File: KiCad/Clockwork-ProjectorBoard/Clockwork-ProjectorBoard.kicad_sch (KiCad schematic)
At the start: 32 parts, among them J1 to TCA955 PCB, J2 to DIN connecting 3+1 Socket 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, J3 to Lamp Relay Board, J4 to DIN Socket traces, J5 Relais Board, J6 uC Cable, J7 DIN-6 female, Q1 AO3400A, U1 AP63205WU, U3 TS5A3160DBVR-TP, U4 TS5A3160DBVR-TP, U5 TSV911ILT

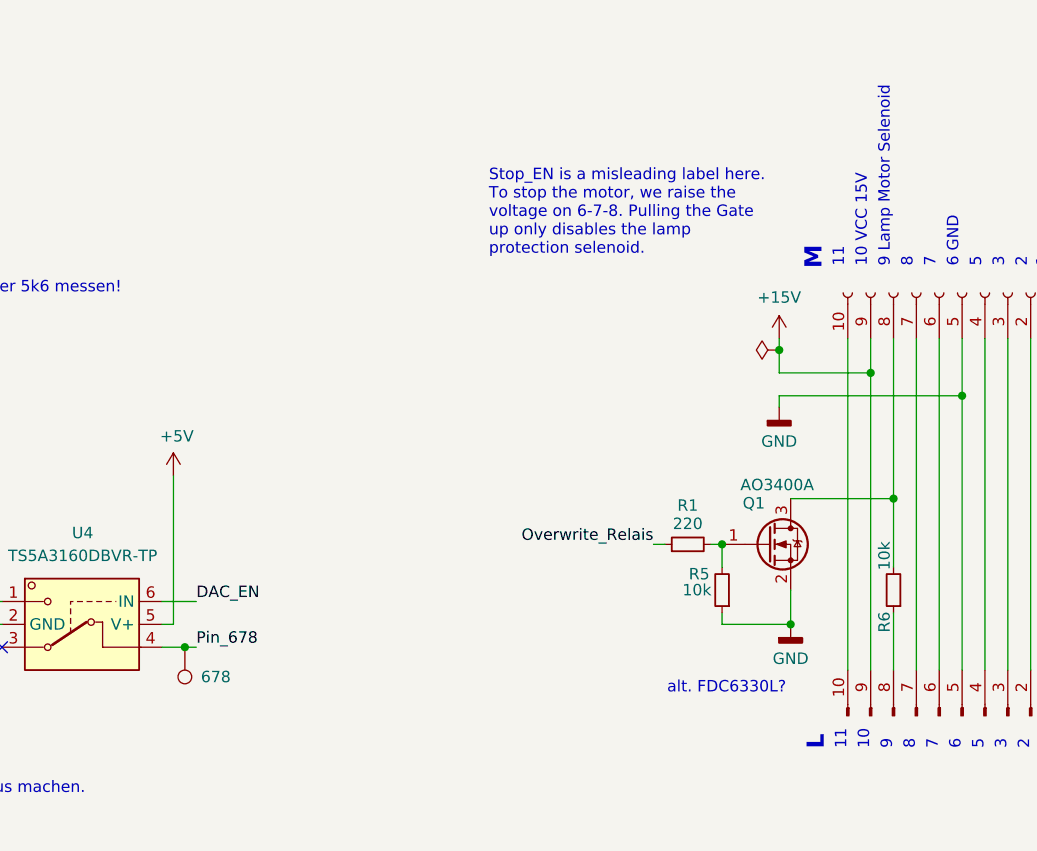
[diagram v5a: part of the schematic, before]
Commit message: Optimize Projector Board Size, red socket will fit better.
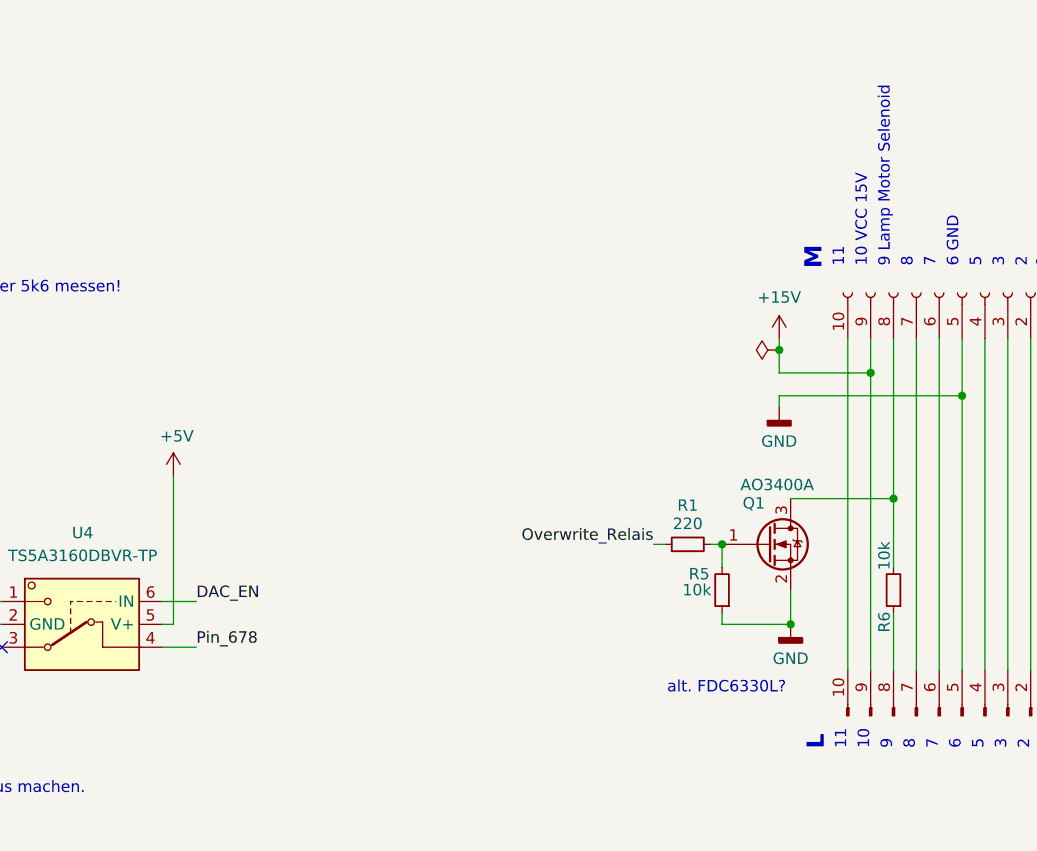
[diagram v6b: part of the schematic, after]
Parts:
- removed TP1: 678, TestPoint:TestPoint_Pad_D1.0mm, symbol Peacemans Teile:TestPoint_named
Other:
- note removed: "Stop_EN is a misleading label here. To stop the motor, we raise the voltage on 6-7-8. Pulling the Gate up only disables the lamp protection selenoid."
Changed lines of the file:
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@@
 	)
 	(junction
-		(at 167.64 130.81)
-		(diameter 0)
-		(color 0 0 0 0)
-	)
-	(junction
 		(at 152.4 43.18)
 		(diameter 0)
@@
 	(wire
 		(pts
-			(xy 168.91 130.81) (xy 167.64 130.81)
+			(xy 165.1 130.81) (xy 168.91 130.81)
 		)
 		(stroke
@@
 	(wire
 		(pts
-			(xy 167.64 130.81) (xy 165.1 130.81)
-		)
-		(stroke
-			(width 0)
-			(type default)
-		)
-	)
-	(wire
-		(pts
 			(xy 243.84 100.33) (xy 243.84 96.52)
 		)
@@
 		)
 	)
-	(text "Stop_EN is a misleading label here.\nTo stop the motor, we raise the \nvoltage on 6-7-8. Pulling the Gate\nup only disables the lamp \nprotection selenoid."
-		(exclude_from_sim no)
-		(at 201.422 82.55 0)
-		(effects
-			(font
-				(size 1.27 1.27)
-			)
-			(justify left)
-		)
-	)
 	(text "2"
 		(exclude_from_sim no)
@@
 					(unit 1)
 				)
-			)
-		)
-	)
-	(symbol
-		(lib_id "Peacemans Teile:TestPoint_named")
-		(at 167.64 130.81 180)
-		(unit 1)
-		(exclude_from_sim no)
-		(in_bom yes)
-		(on_board yes)
-		(dnp no)
-		(property "Reference" "TP1"
-			(at 167.64 137.668 0)
-			(effects
-				(font
-					(size 1.27 1.27)
-				)
-				(hide yes)
-			)
-		)
-		(property "Value" "678"
-			(at 169.418 134.112 0)
-			(effects
-				(font
-					(size 1.27 1.27)
-				)
-				(justify right)
-			)
-		)
-		(property "Footprint" "TestPoint:TestPoint_Pad_D1.0mm"
-			(at 162.56 130.81 0)
-			(effects
-				(font
-					(size 1.27 1.27)
-				)
-				(hide yes)
-			)
-		)
-		(property "Datasheet" "~"
-			(at 162.56 130.81 0)
-			(effects
-				(font
-					(size 1.27 1.27)
-				)
-				(hide yes)
-			)
-		)
-		(property "Description" "test point"
-			(at 167.64 130.81 0)
-			(effects
-				(font
-					(size 1.27 1.27)
-				)
-				(hide yes)
-			)
-		)
-		(property "TP_Label" ""
-			(at 167.64 130.81 0)
-			(effects
-				(font
-					(size 1.27 1.27)
-				)
-			)
-		)
-		(pin "1"
-		)
-		(instances
-			(project "SynCrystal_ProjectorBoard"
-				(path "/01bd7818-adef-4612-bb26-3dbff95808f6"
-					(reference "TP1")
-					(unit 1)
-				)

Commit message: Adding the 6th pin to the Lamp Relay Schematic
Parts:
- J4: LCSC C22388685 -> C7429633
